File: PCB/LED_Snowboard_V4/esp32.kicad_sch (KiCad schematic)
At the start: 22 parts

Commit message: Transfer PCB To Desktop
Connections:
- net RESET: now reaches U1.1 (EN)
- net RESET: now also TP52.1
- net DATA_3: now reaches U1.11 (G14)
- net DATA_3: now also TP8.1
- net DATA_1: now reaches U1.12 (G12)
- net DATA_1: now also TP4.1
- net DATA_2: now reaches U1.13 (G13)
- net DATA_2: now also TP7.1
- net MOSI: now reaches U1.16 (G23)
- net MOSI: now also TP14.1
- net SCL: now reaches U1.17 (G22)
- net SCL: now also TP25.1
- net SENSOR: now reaches U1.2 (G36)
- net SENSOR: now also TP53.1
- net SDA: now reaches U1.20 (G21)
- net SDA: now also TP26.1
- net MISO: now reaches U1.21 (G19)
- net MISO: now also TP13.1
- net SCLK: now reaches U1.22 (G18)
- net SCLK: now also TP19.1
- net CS: now reaches U1.23 (G5)
- net CS: now also TP20.1
- net TX: now reaches U1.24 (G17)
- net TX: now also TP31.1
- net RX: now reaches U1.25 (G16)
- net RX: now also TP32.1
- net INT: now reaches U1.4 (G34)
- net INT: now also TP58.1
- net GATE_SIGNAL: now reaches U1.6 (G32)
- net GATE_SIGNAL: now also TP1.1
- net SD_SW: now reaches U1.8 (G25)
- net SD_SW: now also TP59.1
- no-connect marks 0 -> 5
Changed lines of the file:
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@@
 (kicad_sch (version 20230121) (generator eeschema)
   (paper "A4")
+  (no_connect (at 168.91 104.14))
+  (no_connect (at 168.91 101.6))
+  (no_connect (at 168.91 81.28))
+  (no_connect (at 168.91 99.06))
+  (no_connect (at 168.91 78.74))
+  (wire (pts (xy 31.75 143.51) (xy 41.91 143.51))
+    (stroke (width 0) (type default))
+  )
+  (wire (pts (xy 143.51 104.14) (xy 133.35 104.14))
+    (stroke (width 0) (type default))
+  )
+  (wire (pts (xy 31.75 55.88) (xy 41.91 55.88))
+    (stroke (width 0) (type default))
+  )
   (wire (pts (xy 33.02 44.45) (xy 33.02 45.72))
     (stroke (width 0) (type default))
@@
     (stroke (width 0) (type default))
   )
+  (wire (pts (xy 31.75 153.67) (xy 41.91 153.67))
+    (stroke (width 0) (type default))
+  )
   (wire (pts (xy 34.29 24.13) (xy 34.29 21.59))
     (stroke (width 0) (type default))
   )
+  (wire (pts (xy 31.75 86.36) (xy 41.91 86.36))
+    (stroke (width 0) (type default))
+  )
+  (wire (pts (xy 168.91 93.98) (xy 179.07 93.98))
+    (stroke (width 0) (type default))
+  )
+  (wire (pts (xy 168.91 96.52) (xy 179.07 96.52))
+    (stroke (width 0) (type default))
+  )
+  (wire (pts (xy 31.75 81.28) (xy 41.91 81.28))
+    (stroke (width 0) (type default))
+  )
   (wire (pts (xy 45.72 34.29) (xy 31.75 34.29))
     (stroke (width 0) (type default))
   )
+  (wire (pts (xy 168.91 86.36) (xy 179.07 86.36))
+    (stroke (width 0) (type default))
+  )
+  (wire (pts (xy 168.91 83.82) (xy 179.07 83.82))
+    (stroke (width 0) (type default))
+  )
   (wire (pts (xy 31.75 39.37) (xy 50.8 39.37))
     (stroke (width 0) (type default))
   )
+  (wire (pts (xy 143.51 101.6) (xy 133.35 101.6))
+    (stroke (width 0) (type default))
+  )
   (wire (pts (xy 45.72 21.59) (xy 45.72 34.29))
     (stroke (width 0) (type default))
   )
+  (wire (pts (xy 168.91 91.44) (xy 179.07 91.44))
+    (stroke (width 0) (type default))
+  )
+  (wire (pts (xy 168.91 88.9) (xy 179.07 88.9))
+    (stroke (width 0) (type default))
+  )
+  (wire (pts (xy 143.51 81.28) (xy 133.35 81.28))
+    (stroke (width 0) (type default))
+  )
+  (wire (pts (xy 31.75 121.92) (xy 41.91 121.92))
+    (stroke (width 0) (type default))
+  )
+  (wire (pts (xy 31.75 66.04) (xy 41.91 66.04))
+    (stroke (width 0) (type default))
+  )
+  (wire (pts (xy 31.75 138.43) (xy 41.91 138.43))
+    (stroke (width 0) (type default))
+  )
+  (wire (pts (xy 143.51 91.44) (xy 133.35 91.44))
+    (stroke (width 0) (type default))
+  )
+  (wire (pts (xy 31.75 127) (xy 41.91 127))
+    (stroke (width 0) (type default))
+  )
+  (wire (pts (xy 31.75 91.44) (xy 41.91 91.44))
+    (stroke (width 0) (type default))
+  )
+  (wire (pts (xy 31.75 96.52) (xy 41.91 96.52))
+    (stroke (width 0) (type default))
+  )
   (wire (pts (xy 40.64 29.21) (xy 31.75 29.21))
     (stroke (width 0) (type default))
   )
+  (wire (pts (xy 143.51 99.06) (xy 133.35 99.06))
+    (stroke (width 0) (type default))
+  )
   (wire (pts (xy 31.75 44.45) (xy 33.02 44.45))
     (stroke (width 0) (type default))
   )
+  (wire (pts (xy 143.51 86.36) (xy 133.35 86.36))
+    (stroke (width 0) (type default))
+  )
+  (wire (pts (xy 31.75 110.49) (xy 41.91 110.49))
+    (stroke (width 0) (type default))
+  )
+  (wire (pts (xy 143.51 73.66) (xy 133.35 73.66))
+    (stroke (width 0) (type default))
+  )
+  (wire (pts (xy 31.75 71.12) (xy 41.91 71.12))
+    (stroke (width 0) (type default))
+  )
   (wire (pts (xy 50.8 39.37) (xy 50.8 21.59))
     (stroke (width 0) (type default))
   )
+  (wire (pts (xy 168.91 76.2) (xy 179.07 76.2))
+    (stroke (width 0) (type default))
+  )
+  (wire (pts (xy 143.51 76.2) (xy 133.35 76.2))
+    (stroke (width 0) (type default))
+  )
+  (wire (pts (xy 31.75 148.59) (xy 41.91 148.59))
+    (stroke (width 0) (type default))
+  )
+  (wire (pts (xy 168.91 73.66) (xy 179.07 73.66))
+    (stroke (width 0) (type default))
+  )
   (wire (pts (xy 40.64 21.59) (xy 40.64 29.21))
     (stroke (width 0) (type default))
   )
+  (wire (pts (xy 31.75 60.96) (xy 41.91 60.96))
+    (stroke (width 0) (type default))
+  )
+  (wire (pts (xy 31.75 105.41) (xy 41.91 105.41))
+    (stroke (width 0) (type default))
+  )
+  (hierarchical_label "GATE_SIGNAL" (shape input) (at 41.91 55.88 0) (fields_autoplaced)
+    (effects (font (size 1.27 1.27)) (justify left))
+  )
+  (hierarchical_label "SDA" (shape input) (at 179.07 83.82 0) (fields_autoplaced)
+    (effects (font (size 1.27 1.27)) (justify left))
+  )
+  (hierarchical_label "DATA_1" (shape input) (at 133.35 101.6 180) (fields_autoplaced)
+    (effects (font (size 1.27 1.27)) (justify right))
+  )
+  (hierarchical_label "SDA" (shape input) (at 41.91 110.49 0) (fields_autoplaced)
+    (effects (font (size 1.27 1.27)) (justify left))
+  )
+  (hierarchical_label "DATA_3" (shape input) (at 41.91 71.12 0) (fields_autoplaced)
+    (effects (font (size 1.27 1.27)) (justify left))
+  )
+  (hierarchical_label "SCL" (shape input) (at 179.07 76.2 0) (fields_autoplaced)
+    (effects (font (size 1.27 1.27)) (justify left))
+  )
+  (hierarchical_label "SD_SW" (shape input) (at 41.91 153.67 0) (fields_autoplaced)
+    (effects (font (size 1.27 1.27)) (justify left))
+  )
+  (hierarchical_label "TX" (shape input) (at 179.07 93.98 0) (fields_autoplaced)
+    (effects (font (size 1.27 1.27)) (justify left))
+  )
+  (hierarchical_label "INT" (shape input) (at 41.91 148.59 0) (fields_autoplaced)
+    (effects (font (size 1.27 1.27)) (justify left))
+  )
+  (hierarchical_label "SCL" (shape input) (at 41.91 105.41 0) (fields_autoplaced)
+    (effects (font (size 1.27 1.27)) (justify left))
+  )
+  (hierarchical_label "DATA_2" (shape input) (at 41.91 66.04 0) (fields_autoplaced)
+    (effects (font (size 1.27 1.27)) (justify left))
+  )
+  (hierarchical_label "SD_SW" (shape input) (at 133.35 91.44 180) (fields_autoplaced)
+    (effects (font (size 1.27 1.27)) (justify right))
+  )
+  (hierarchical_label "TX" (shape input) (at 41.91 121.92 0) (fields_autoplaced)
+    (effects (font (size 1.27 1.27)) (justify left))
+  )
+  (hierarchical_label "RX" (shape input) (at 179.07 96.52 0) (fields_autoplaced)
+    (effects (font (size 1.27 1.27)) (justify left))
+  )
+  (hierarchical_label "MISO" (shape input) (at 179.07 86.36 0) (fields_autoplaced)
+    (effects (font (size 1.27 1.27)) (justify left))
+  )
+  (hierarchical_label "CS" (shape input) (at 41.91 96.52 0) (fields_autoplaced)
+    (effects (font (size 1.27 1.27)) (justify left))
+  )
+  (hierarchical_label "DATA_1" (shape input) (at 41.91 60.96 0) (fields_autoplaced)
+    (effects (font (size 1.27 1.27)) (justify left))
+  )
+  (hierarchical_label "GATE_SIGNAL" (shape input) (at 133.35 86.36 180) (fields_autoplaced)
+    (effects (font (size 1.27 1.27)) (justify right))
+  )
+  (hierarchical_label "SCLK" (shape input) (at 41.91 91.44 0) (fields_autoplaced)
+    (effects (font (size 1.27 1.27)) (justify left))
+  )
+  (hierarchical_label "INT" (shape input) (at 133.35 81.28 180) (fields_autoplaced)
+    (effects (font (size 1.27 1.27)) (justify right))
+  )
+  (hierarchical_label "RESET" (shape input) (at 41.91 138.43 0) (fields_autoplaced)
+    (effects (font (size 1.27 1.27)) (justify left))
+  )
+  (hierarchical_label "RESET" (shape input) (at 133.35 73.66 180) (fields_autoplaced)
+    (effects (font (size 1.27 1.27)) (justify right))
+  )
+  (hierarchical_label "SCLK" (shape input) (at 179.07 88.9 0) (fields_autoplaced)
+    (effects (font (size 1.27 1.27)) (justify left))
+  )
+  (hierarchical_label "SENSOR" (shape input) (at 41.91 143.51 0) (fields_autoplaced)
+    (effects (font (size 1.27 1.27)) (justify left))
+  )
+  (hierarchical_label "DATA_3" (shape input) (at 133.35 99.06 180) (fields_autoplaced)
+    (effects (font (size 1.27 1.27)) (justify right))
+  )
+  (hierarchical_label "MISO" (shape input) (at 41.91 81.28 0) (fields_autoplaced)
+    (effects (font (size 1.27 1.27)) (justify left))
+  )
+  (hierarchical_label "DATA_2" (shape input) (at 133.35 104.14 180) (fields_autoplaced)
+    (effects (font (size 1.27 1.27)) (justify right))
+  )
+  (hierarchical_label "MOSI" (shape input) (at 179.07 73.66 0) (fields_autoplaced)
+    (effects (font (size 1.27 1.27)) (justify left))
+  )
+  (hierarchical_label "MOSI" (shape input) (at 41.91 86.36 0) (fields_autoplaced)
+    (effects (font (size 1.27 1.27)) (justify left))
+  )
+  (hierarchical_label "RX" (shape input) (at 41.91 127 0) (fields_autoplaced)
+    (effects (font (size 1.27 1.27)) (justify left))
+  )
+  (hierarchical_label "SENSOR" (shape input) (at 133.35 76.2 180) (fields_autoplaced)
+    (effects (font (size 1.27 1.27)) (justify right))
+  )
+  (hierarchical_label "CS" (shape input) (at 179.07 91.44 0) (fields_autoplaced)
+    (effects (font (size 1.27 1.27)) (justify left))
+  )
   (symbol (lib_id "Connector:TestPoint_Alt") (at 31.75 39.37 90) (unit 1)

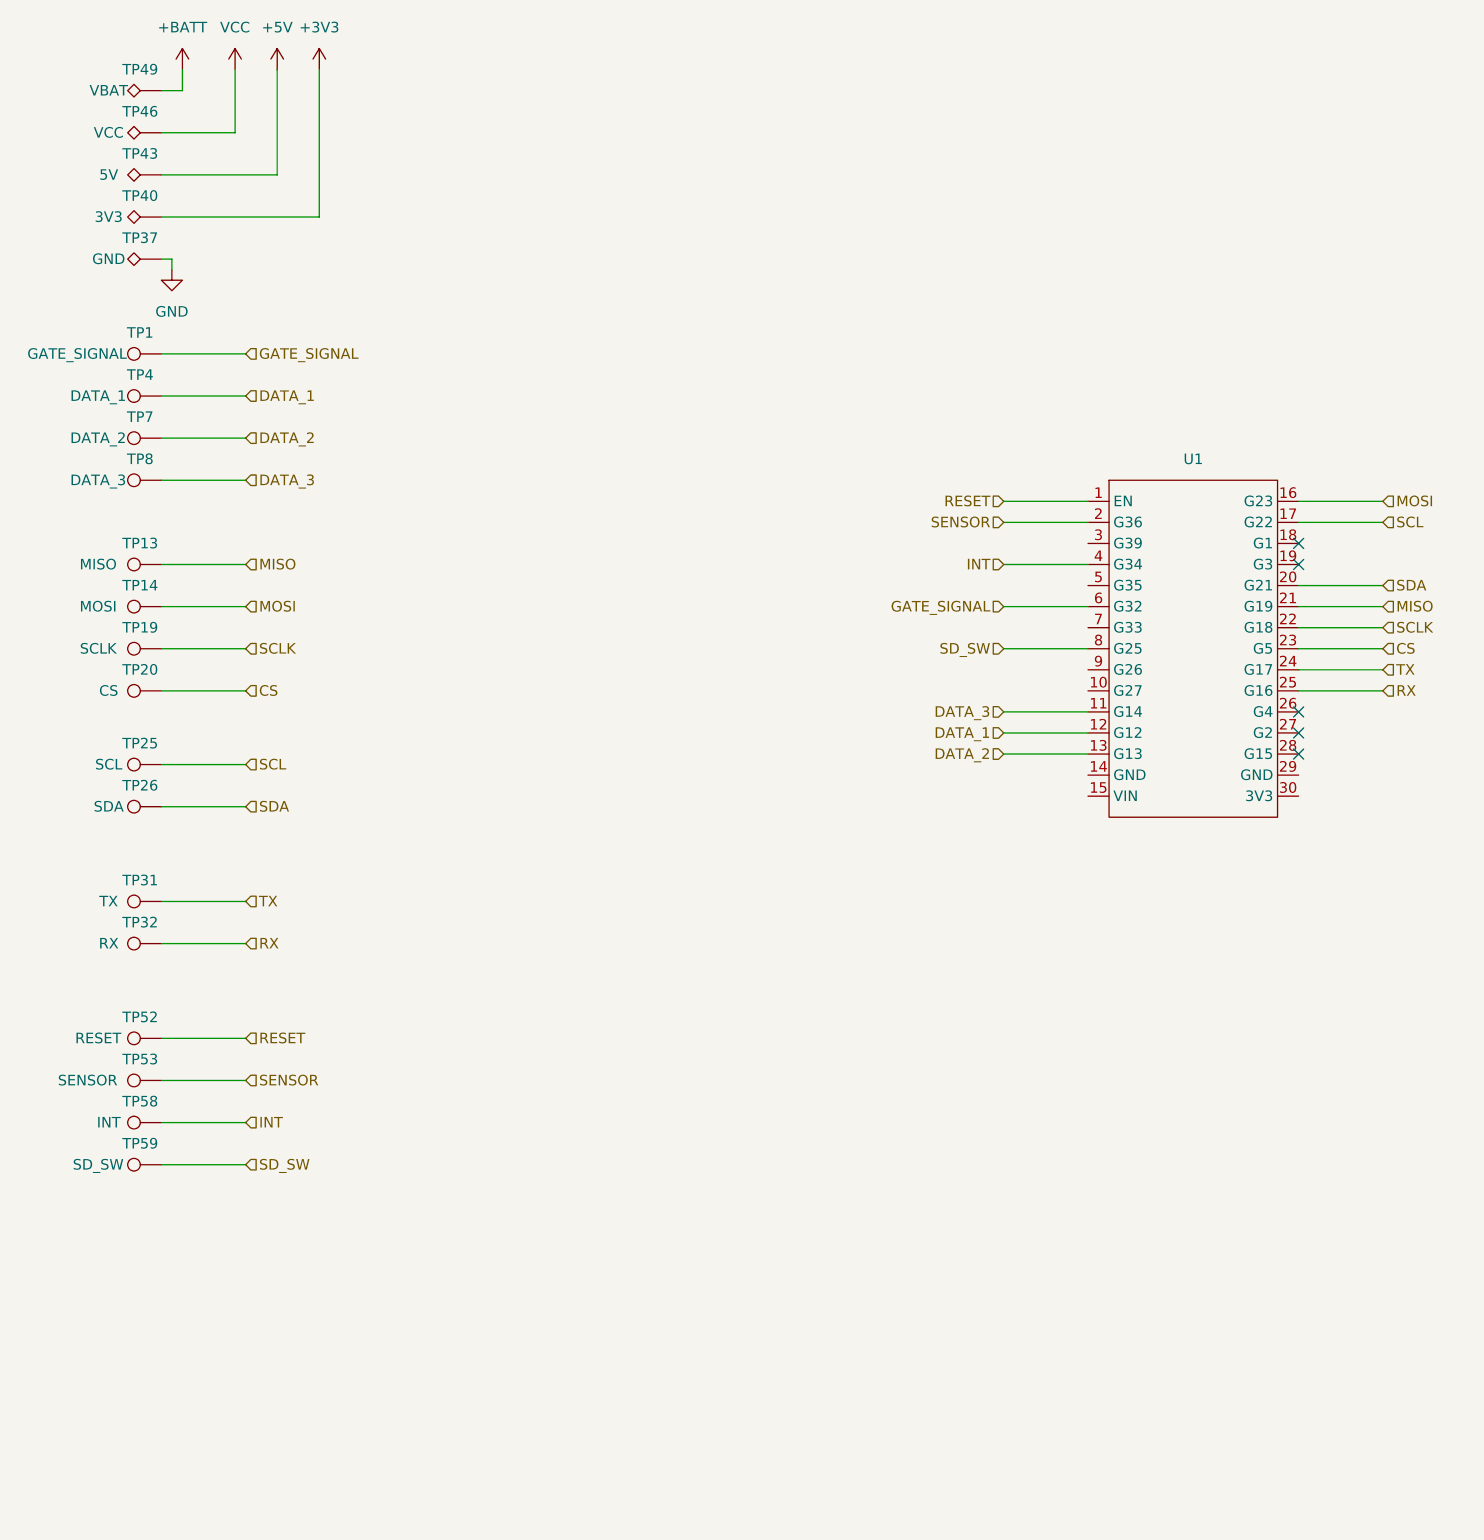
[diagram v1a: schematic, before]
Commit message: Post Review
Reviewed with Tim. need to add power line protections. settled on no battery heater for now
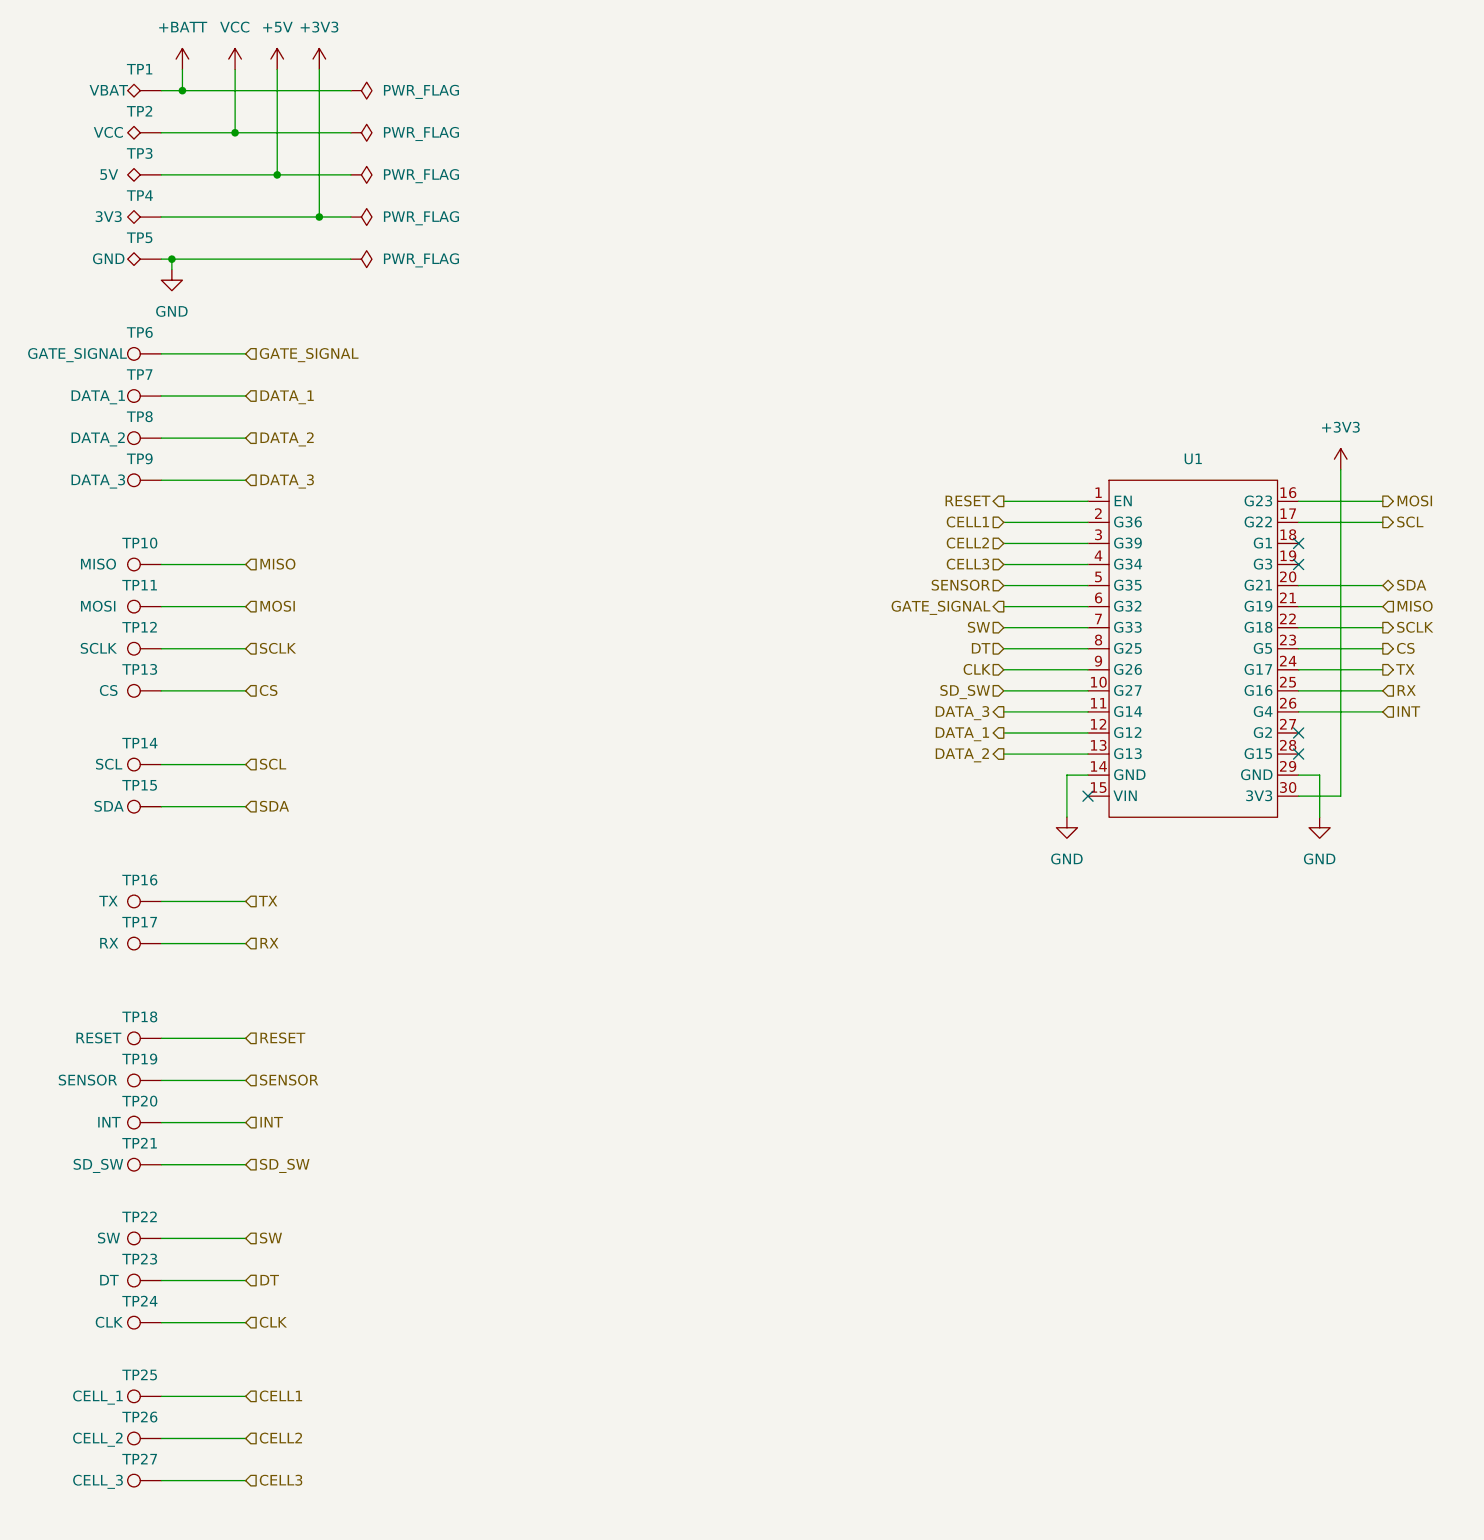
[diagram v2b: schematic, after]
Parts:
- added TP22: SW, symbol Connector:TestPoint
- added TP23: DT, symbol Connector:TestPoint
- added TP24: CLK, symbol Connector:TestPoint
- added TP25: CELL_1, symbol Connector:TestPoint
- added TP26: CELL_2, symbol Connector:TestPoint
- added TP27: CELL_3, symbol Connector:TestPoint
- renumbered TP49 to TP1, TP13 to TP10, TP14 to TP11, TP19 to TP12, TP20 to TP13, TP25 to TP14, TP26 to TP15, TP31 to TP16, TP32 to TP17, TP52 to TP18, TP53 to TP19, TP46 to TP2, TP58 to TP20, TP59 to TP21, TP43 to TP3, TP40 to TP4, TP37 to TP5, TP1 to TP6, TP4 to TP7, TP7 to TP8, TP8 to TP9
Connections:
- net +3V3: now also U1.30 (3V3)
- net GND: now also U1.14 (GND), U1.29 (GND)
- net INT: now also U1.26 (G4); no longer U1.4 (G34)
- net SD_SW: now also U1.10 (G27); no longer U1.8 (G25)
- net SENSOR: now also U1.5 (G35); no longer U1.2 (G36)
- net CELL2: now reaches U1.3 (G39)
- net CELL2: now also TP26.1
- net SW: now reaches U1.7 (G33)
- net SW: now also TP22.1
- net CLK: now reaches U1.9 (G26)
- net CLK: now also TP24.1
- new net CELL1: TP25.1, U1.2 (G36)
- new net CELL3: TP27.1, U1.4 (G34)
- new net DT: TP23.1, U1.8 (G25)
